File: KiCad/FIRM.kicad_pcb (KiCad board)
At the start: 4 copper layers, 38.5 x 38.5 mm, 98 parts, among them J1 Conn_01x02_Pin, J2 DM3CS-SF, Q2 IRLML6402, SW1 PTS815, U1 STM32F405RGTx, U2 MIC5219-3.3YM5, U6 A-USBC-20F0-EA-GSR05, U7 W25Q128JVS, X2 32.768khz, Y1 12 MHz

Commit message: backup
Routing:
- net /SDIO_D3: track 29.9 -> 29.1 mm
- net /PB4: track 32.2 -> 32.9 mm

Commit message: almost done
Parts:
- moved C4 30.9 mm to (139.1, 111.0), turned to 90 degrees
- moved R14 29.1 mm to (134.4, 105.8), turned to 0 degrees
- moved C25 26.8 mm to (136.2, 108.3)
- moved U7 26.2 mm to (136.6, 111.6), turned to -90 degrees
- moved R21 26.0 mm to (136.7, 112.1), turned to 0 degrees
- moved C5 25.8 mm to (117.2, 125.7)
- moved R13 25.2 mm to (133.1, 104.0), turned to 180 degrees
- moved TP16 15.6 mm to (112.8, 101.5)
- moved TP15 13.9 mm to (110.3, 101.5)
- moved D4 10.6 mm to (109.0, 116.5), turned to 90 degrees
- moved C18 9.86 mm to (107.0, 134.0)
- moved JP1 9.86 mm to (106.5, 136.5)
- moved JP2 9.86 mm to (110.0, 136.5)
- moved JP3 9.86 mm to (110.8, 132.8)
- moved JP4 9.86 mm to (110.8, 129.8)
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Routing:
- net GND: track 107.1 -> 0.00 mm, vias 48 -> 0
- net +3.3V: track 59.1 -> 1.14 mm, vias 27 -> 1
- net /PA2: track 56.0 -> 0.00 mm, vias 4 -> 0
- net /PA0: track 43.2 -> 0.00 mm, vias 3 -> 0
- net /PA8: track 41.6 -> 0.00 mm, vias 6 -> 0
- net /PA1: track 36.7 -> 0.00 mm, vias 1 -> 0
- net /PB11: track 34.5 -> 0.00 mm, vias 3 -> 0
- net /PB4: track 32.9 -> 0.00 mm, vias 3 -> 0
- net /PA3: track 32.3 -> 0.00 mm, vias 2 -> 0
- net /PB10: track 32.0 -> 0.00 mm, vias 2 -> 0
- net /PA4: track 31.8 -> 0.00 mm, vias 6 -> 0
- net /PB5: track 31.5 -> 0.00 mm, vias 8 -> 0
- net /PB8: track 26.0 -> 0.00 mm, vias 6 -> 0
- net /PC13: track 25.9 -> 0.00 mm, vias 2 -> 0
- net /PB3: track 25.6 -> 0.00 mm, vias 2 -> 0
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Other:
- board size 38.5 x 38.5 mm -> 40.5 x 40.5 mm

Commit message: chat we are so back
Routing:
- net GND: track 0.00 -> 96.1 mm, vias 0 -> 47
- net /PA8: track 0.00 -> 64.7 mm, vias 0 -> 7
- net +3.3V: track 1.14 -> 55.3 mm, vias 1 -> 33
- net /PA1: track 0.00 -> 44.8 mm, vias 0 -> 5
- net /PB10: track 0.00 -> 41.1 mm, vias 0 -> 2
- net /PB11: track 0.00 -> 39.9 mm, vias 0 -> 2
- net /PA2: track 0.00 -> 36.4 mm, vias 0 -> 4
- net /PC0: track 0.00 -> 31.9 mm, vias 0 -> 2
- net /PA0: track 0.00 -> 31.8 mm, vias 0 -> 2
- net /PA4: track 0.00 -> 31.3 mm, vias 0 -> 6
- net /PA3: track 0.00 -> 30.9 mm, vias 0 -> 2
- net /PC13: track 0.00 -> 28.8 mm, vias 0 -> 2
- net /PC1: track 0.00 -> 24.6 mm, vias 0 -> 6
- net /PB5: track 0.00 -> 21.6 mm, vias 0 -> 2
- net /PB4: track 0.00 -> 19.0 mm, vias 0 -> 2
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
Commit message: silkscreen
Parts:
- moved SDA 0.50 mm to (107.0, 136.5)
- renumbered TP28 to 3.3V, TP4 to A0, TP5 to A1, TP11 to A10, TP12 to A15, TP6 to A2, TP7 to A3, TP8 to A4, TP9 to A8, TP10 to A9, TP17 to B10, TP18 to B11, TP13 to B3, TP14 to B4, TP15 to B5, TP16 to B8, J1 to BAT, TP25 to BOOT0, TP29 to C0, TP30 to C1, TP24 to C13, TP26 to GND, TP1 to GND, TP27 to GND, JP2 to MOSI, SW1 to RST, JP4 to SCK, JP3 to SCL, JP1 to SDA, TP3 to SWCLK, TP2 to SWDIO, J2 to U5
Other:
- board text added: "You Firmed Up Yet?"

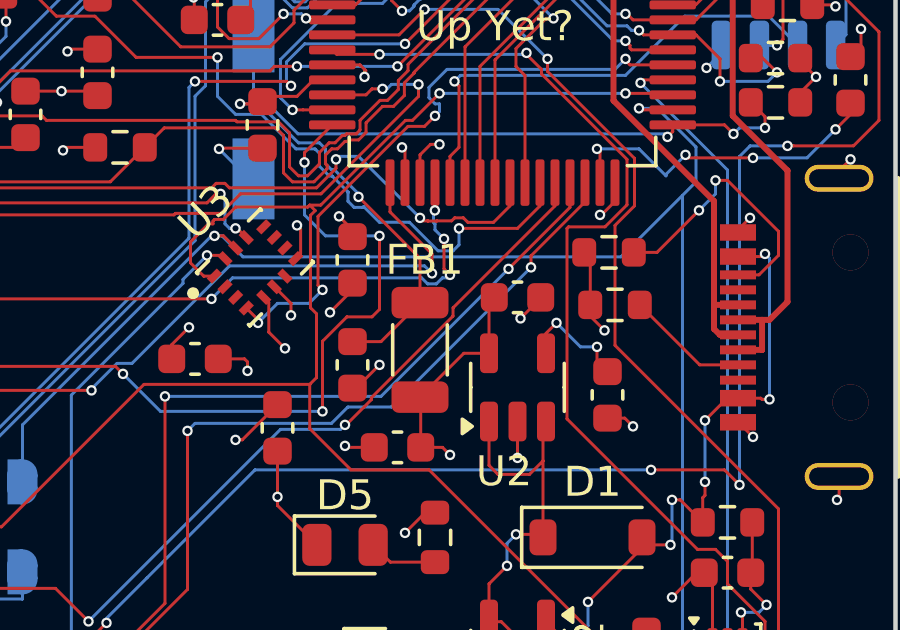
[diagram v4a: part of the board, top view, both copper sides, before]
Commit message: fix fb and cap
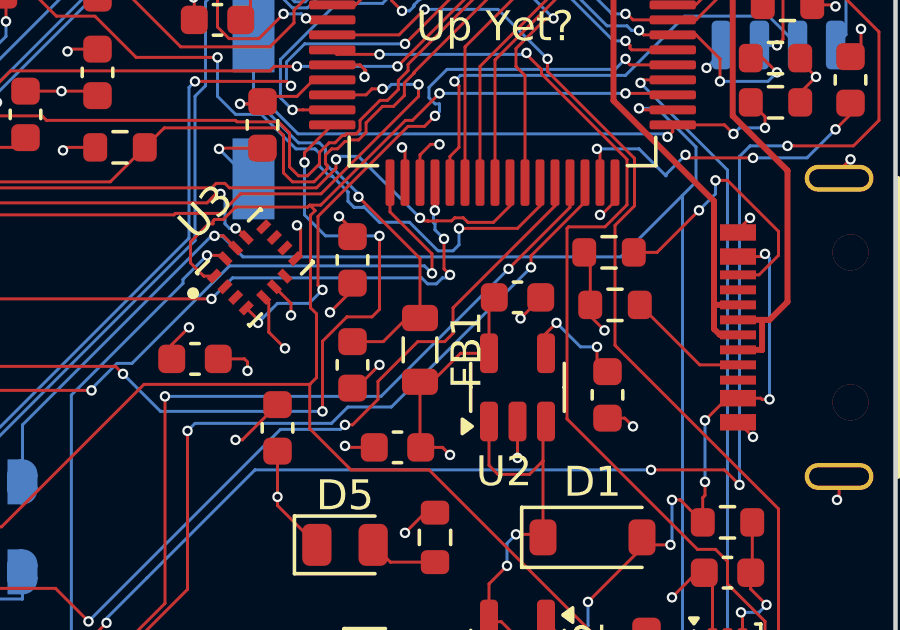
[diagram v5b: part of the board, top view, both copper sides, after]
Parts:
- FB1: footprint Inductor_SMD:L_1206_3216Metric -> Inductor_SMD:L_0805_2012Metric
- renumbered U5 to J2, C13 to TP24, C1 to TP30
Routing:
- net /MAG_INT: track 34.7 -> 35.4 mm
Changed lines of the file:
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@@
 		(descr "THT rectangular pad as test Point, square 1.5mm side length, hole diameter 0.7mm")
 		(tags "test point THT pad rectangle square")
-		(property "Reference" "C1"
+		(property "Reference" "TP30"
 			(at 0 -2.14 90)
 			(layer "B.SilkS")
@@
 		)
 	)
-	(footprint "Inductor_SMD:L_1206_3216Metric"
+	(footprint "Inductor_SMD:L_0805_2012Metric"
 		(layer "F.Cu")
 		(at 124.65 125.35 -90)
-		(descr "Inductor SMD 1206 (3216 Metric), square (rectangular) end terminal, IPC-7351 nominal, (Body size source: IPC-SM-782 page 80, https://www.pcb-3d.com/wordpress/wp-content/uploads/ipc-sm-782a_amendment_1_and_2.pdf), generated with kicad-footprint-generator")
+		(descr "Inductor SMD 0805 (2012 Metric), square (rectangular) end terminal, IPC-7351 nominal, (Body size source: IPC-SM-782 page 80, https://www.pcb-3d.com/wordpress/wp-content/uploads/ipc-sm-782a_amendment_1_and_2.pdf), generated with kicad-footprint-generator")
 		(tags "inductor")
 		(property "Reference" "FB1"
-			(at -3 -0.15 180)
+			(at 0 -1.55 270)
 			(layer "F.SilkS")
 			(effects
@@
 		)
 		(property "Value" "120 Ohms @ 100 MHz"
-			(at 0 1.9 90)
+			(at 0 1.55 270)
 			(layer "F.Fab")
 			(effects
@@
 		)
 		(property "Datasheet" "https://fair-rite.com/product/chip-beads-2508051217y6/"
-			(at 0 0 90)
+			(at 0 0 270)
 			(layer "F.Fab")
 			(hide yes)
@@
 		)
 		(property "Description" "2508051217Y6"
-			(at 0 0 90)
+			(at 0 0 270)
 			(layer "F.Fab")
 			(hide yes)
@@
 		(attr smd)
 		(fp_line
-			(start -0.835242 0.91)
-			(end 0.835242 0.91)
+			(start -0.399622 0.56)
+			(end 0.399622 0.56)
 			(stroke
 				(width 0.12)
@@
 		)
 		(fp_line
-			(start -0.835242 -0.91)
-			(end 0.835242 -0.91)
+			(start -0.399622 -0.56)
+			(end 0.399622 -0.56)
 			(stroke
 				(width 0.12)
@@
 		)
 		(fp_line
-			(start -2.35 1.2)
-			(end -2.35 -1.2)
+			(start -1.75 0.85)
+			(end -1.75 -0.85)
 			(stroke
 				(width 0.05)
@@
 		)
 		(fp_line
-			(start 2.35 1.2)
-			(end -2.35 1.2)
+			(start 1.75 0.85)
+			(end -1.75 0.85)
 			(stroke
 				(width 0.05)
@@
 		)
 		(fp_line
-			(start -2.35 -1.2)
-			(end 2.35 -1.2)
+			(start -1.75 -0.85)
+			(end 1.75 -0.85)
 			(stroke
 				(width 0.05)
@@
 		)
 		(fp_line
-			(start 2.35 -1.2)
-			(end 2.35 1.2)
+			(start 1.75 -0.85)
+			(end 1.75 0.85)
 			(stroke
 				(width 0.05)
@@
 		)
 		(fp_line
-			(start -1.6 0.8)
-			(end -1.6 -0.8)
+			(start -1 0.45)
+			(end -1 -0.45)
 			(stroke
 				(width 0.1)
@@
 		)
 		(fp_line
-			(start 1.6 0.8)
-			(end -1.6 0.8)
+			(start 1 0.45)
+			(end -1 0.45)
 			(stroke
 				(width 0.1)
@@
 		)
 		(fp_line
-			(start -1.6 -0.8)
-			(end 1.6 -0.8)
+			(start -1 -0.45)
+			(end 1 -0.45)
 			(stroke
 				(width 0.1)
@@
 		)
 		(fp_line
-			(start 1.6 -0.8)
-			(end 1.6 0.8)
+			(start 1 -0.45)
+			(end 1 0.45)
 			(stroke
 				(width 0.1)
@@
 		)
 		(fp_text user "${REFERENCE}"
-			(at 0 0 90)
+			(at 0 0 270)
 			(layer "F.Fab")
 			(effects
 				(font
-					(size 0.8 0.8)
-					(thickness 0.12)
+					(size 0.5 0.5)
+					(thickness 0.08)
 				)
 			)
 		)
 		(pad "1" smd roundrect
-			(at -1.575 0 270)
-			(size 1.05 1.9)
+			(at -1.0625 0 270)
+			(size 0.875 1.2)
 			(layers "F.Cu" "F.Mask" "F.Paste")
-			(roundrect_rratio 0.238095)
+			(roundrect_rratio 0.25)
 			(net 3 "Net-(U1-VDDA)")
 			(pintype "passive")
 		)
 		(pad "2" smd roundrect
-			(at 1.575 0 270)
-			(size 1.05 1.9)
+			(at 1.0625 0 270)
+			(size 0.875 1.2)
 			(layers "F.Cu" "F.Mask" "F.Paste")
-			(roundrect_rratio 0.238095)
+			(roundrect_rratio 0.25)
 			(net 1 "+3.3V")
 			(pintype "passive")
 		)
 		(embedded_fonts no)
-		(model "${KICAD9_3DMODEL_DIR}/Inductor_SMD.3dshapes/L_1206_3216Metric.step"
+		(model "${KICAD9_3DMODEL_DIR}/Inductor_SMD.3dshapes/L_0805_2012Metric.step"
 			(offset
 				(xyz 0 0 0)
@@
 		(descr "THT rectangular pad as test Point, square 1.5mm side length, hole diameter 0.7mm")
 		(tags "test point THT pad rectangle square")
-		(property "Reference" "C13"
+		(property "Reference" "TP24"
 			(at 0.01 -2.87 0)
 			(layer "B.SilkS")
@@
 		(layer "B.Cu")
 		(at 112.75 116.55 90)
-		(property "Reference" "U5"
+		(property "Reference" "J2"
 			(at 0 8.39 90)
 			(layer "B.SilkS")
@@
 	)
 	(segment
+		(start 125.05 126.4125)
+		(end 126 125.4625)
+		(width 0.1)
+		(layer "F.Cu")
+		(net 1)
+	)
+	(segment
 		(start 131.15 120.4)
 		(end 130.7 120.85)
@@
 	)
 	(segment
+		(start 124.65 126.4125)
+		(end 125.05 126.4125)
+		(width 0.1)
+		(layer "F.Cu")
+		(net 1)
+	)
+	(segment
 		(start 137.025 107.475)
 		(end 136.55 107)
@@
 	)
 	(segment
-		(start 124.425 105.775)
-		(end 124.45 105.8)
+		(start 126 125.4625)
+		(end 126.95 125.4625)
 		(width 0.1)
 		(layer "F.Cu")
@@
 	)
 	(segment
-		(start 134.4 134.8375)
-		(end 132.3125 134.8375)
+		(start 124.425 105.775)
+		(end 124.45 105.8)
 		(width 0.1)
 		(layer "F.Cu")
@@
 	)
 	(segment
-		(start 126.1125 125.4625)
-		(end 126.95 125.4625)
+		(start 134.4 134.8375)
+		(end 132.3125 134.8375)
 		(width 0.1)
 		(layer "F.Cu")
@@
 	)
 	(segment
-		(start 124.675 128.6)
-		(end 124.675 126.95)
-		(width 0.1)
-		(layer "F.Cu")
-		(net 1)
-	)
-	(segment
-		(start 124.65 126.925)
-		(end 126.1125 125.4625)
-		(width 0.1)
-		(layer "F.Cu")
-		(net 1)
-	)
-	(segment
 		(start 125.3 118.5)
 		(end 125 118.5)
@@
 	)
 	(segment
+		(start 124.675 128.6)
+		(end 124.65 128.575)
+		(width 0.1)
+		(layer "F.Cu")
+		(net 1)
+	)
+	(segment
 		(start 116.375 125.175)
 		(end 116.95 124.6)
@@
 	)
 	(segment
+		(start 124.65 128.575)
+		(end 124.65 126.4125)
+		(width 0.1)
+		(layer "F.Cu")
+		(net 1)
+	)
+	(segment
 		(start 108.15 132.7)
 		(end 107.951 132.899)
@@
 	)
 	(segment
-		(start 124.675 126.95)
-		(end 124.65 126.925)
-		(width 0.1)
-		(layer "F.Cu")
-		(net 1)
-	)
-	(segment
 		(start 112.825 113.625)
 		(end 112.45 113.25)
@@
 	)
 	(segment
-		(start 121.725 116.35)
-		(end 121.1 116.35)
+		(start 124.65 124.2875)
+		(end 124.65 122.3)
 		(width 0.1)
 		(layer "F.Cu")
@@
 	)
 	(segment
-		(start 124.65 123.775)
-		(end 124.65 122.3)
+		(start 121.725 116.35)
+		(end 121.1 116.35)
 		(width 0.1)
 		(layer "F.Cu")
@@
 	)
 	(segment
-		(start 123.35 125.075)
-		(end 124.65 123.775)
+		(start 123.425 125.075)
+		(end 124.2125 124.2875)
 		(width 0.1)
 		(layer "F.Cu")
@@
 	)
 	(segment
-		(start 120.55 116.9)
-		(end 119.575 116.9)
+		(start 124.65 122.3)
+		(end 122.6 120.25)
 		(width 0.1)
 		(layer "F.Cu")
@@
 	)
 	(segment
-		(start 124.65 122.3)
-		(end 122.6 120.25)
+		(start 120.55 116.9)
+		(end 119.575 116.9)
 		(width 0.1)
 		(layer "F.Cu")
@@
 	)
 	(segment
+		(start 118.65 117.15)
+		(end 119.325 117.15)
+		(width 0.1)
+		(layer "F.Cu")
+		(net 3)
+	)
+	(segment
 		(start 122.4 125.075)
-		(end 123.35 125.075)
+		(end 123.425 125.075)
 		(width 0.1)
 		(layer "F.Cu")
@@
 	)
 	(segment
-		(start 118.65 117.15)
-		(end 119.325 117.15)
+		(start 124.2125 124.2875)
+		(end 124.65 124.2875)
 		(width 0.1)
 		(layer "F.Cu")
@@
 	)
 	(segment
-		(start 125.751 124.223028)
-		(end 123.026 126.948028)
+		(start 125.475 125.075)
+		(end 125.751 124.799)
 		(width 0.1)
 		(layer "F.Cu")
@@
 	(segment
 		(start 129.15 120.549999)
-		(end 125.751 123.948999)
+		(end 129.15 119.775)
 		(width 0.1)
 		(layer "F.Cu")
@@
 	)
 	(segment
-		(start 122.187978 127.85)
-		(end 122.15 127.85)
-		(width 0.1)
-		(layer "F.Cu")
-		(net 72)
-	)
-	(segment
-		(start 123.026 126.948028)
-		(end 123.026 127.011978)
+		(start 124.575 125.075)
+		(end 125.475 125.075)
 		(width 0.1)
 		(layer "F.Cu")
@@
 	)
 	(segment
-		(start 129.15 119.775)
-		(end 129.15 120.549999)
-		(width 0.1)
-		(layer "F.Cu")
-		(net 72)
-	)
-	(segment
 		(start 112.5 133.3)
 		(end 107.653611 133.3)
@@
 	)
 	(segment
-		(start 123.026 127.011978)
-		(end 122.187978 127.85)
+		(start 122.15 127.85)
+		(end 122.4 127.85)
+		(width 0.1)
+		(layer "F.Cu")
+		(net 72)
+	)
+	(segment
+		(start 123.25 126.4)
+		(end 124.575 125.075)
+		(width 0.1)
+		(layer "F.Cu")
+		(net 72)
+	)
+	(segment
+		(start 122.4 127.85)
+		(end 123.25 127)
 		(width 0.1)
 		(layer "F.Cu")
@@
 	(segment
 		(start 125.751 123.948999)
-		(end 125.751 124.223028)
+		(end 129.15 120.549999)
+		(width 0.1)
+		(layer "F.Cu")
+		(net 72)
+	)
+	(segment
+		(start 125.751 124.799)
+		(end 125.751 123.948999)
+		(width 0.1)
+		(layer "F.Cu")
+		(net 72)
+	)
+	(segment
+		(start 123.25 127)
+		(end 123.25 126.4)
 		(width 0.1)
 		(layer "F.Cu")

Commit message: refine traces
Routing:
- net /MOSI2: track 65.5 -> 66.3 mm
- net /MAG_INT: track 35.4 -> 34.6 mm

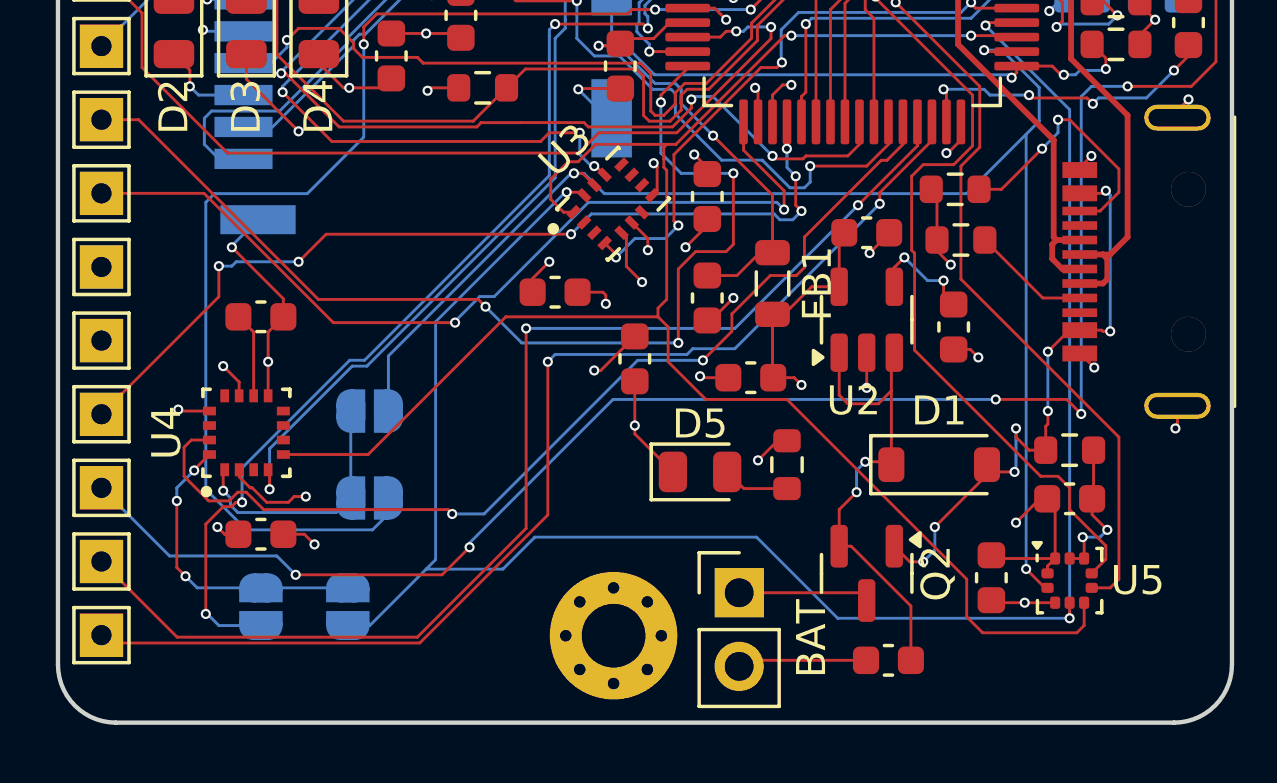
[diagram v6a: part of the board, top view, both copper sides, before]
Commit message: Add silkscreen art, update MMC footprint solder mask expansion
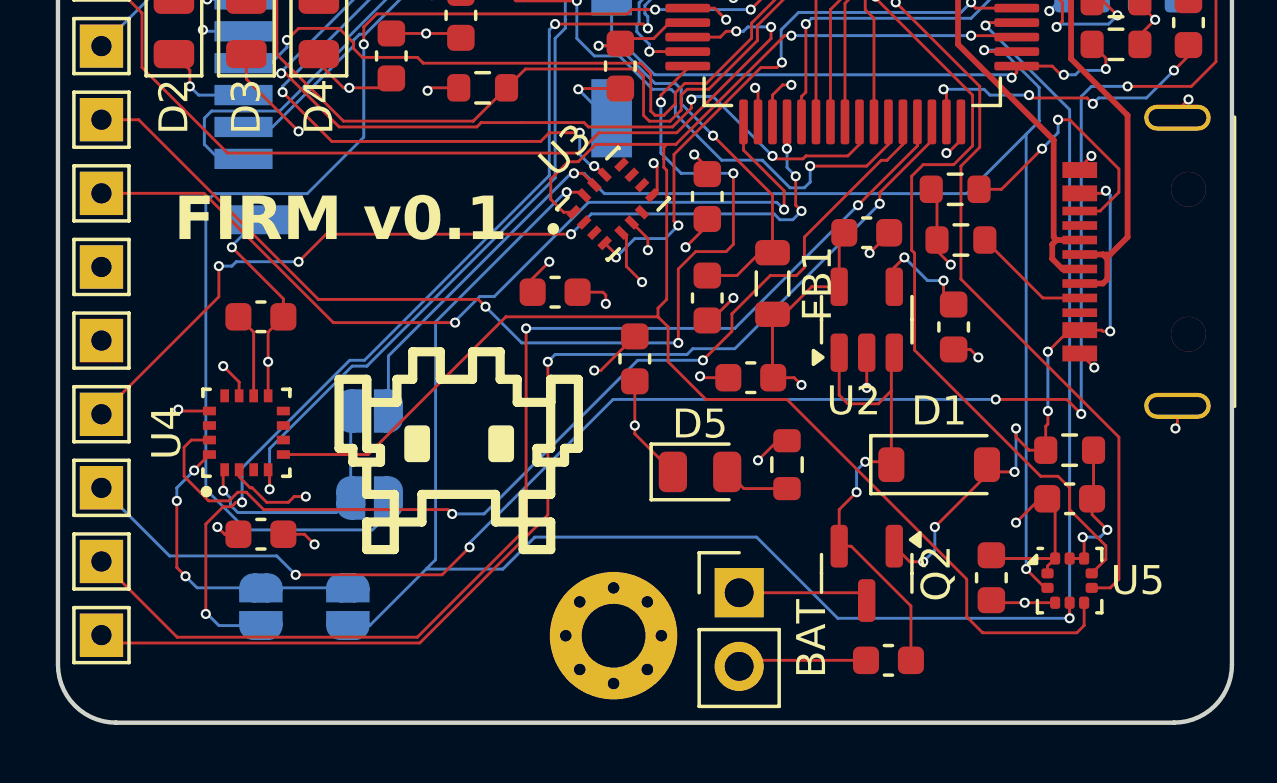
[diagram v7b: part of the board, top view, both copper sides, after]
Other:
- board text added: "FIRM v0.1"
- board text added: "Made FIRM by Will S. Seth O. Craig A. Harshil M."
